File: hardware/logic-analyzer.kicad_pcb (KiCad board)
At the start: 4 copper layers, 39.6 x 40.4 mm, 93 parts, among them J1 USB_C_Receptacle, J2 Conn_02x20, J3 Conn_02x04, J4 Conn_02x15, SW1 SW_Push, SW2 SW_Push, U1 CH32H417MxUx, U16 TPD4EUSB30, U2 Opamp_Dual, U22 TPD4EUSB30, U23 TPD4EUSB30, U3 CH9441P, U4 XC6206PxxxMR, Y1 25MHz 20pF

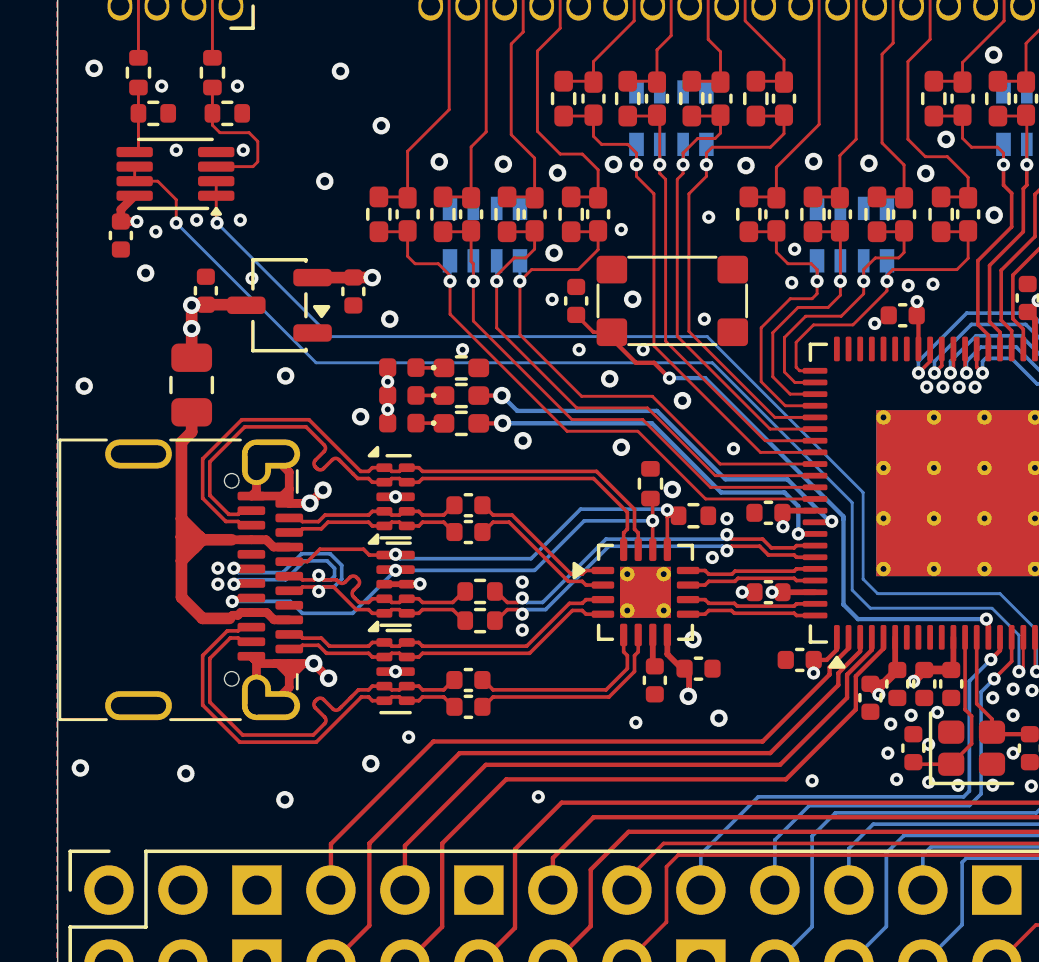
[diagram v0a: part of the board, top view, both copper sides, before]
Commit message: Change CH9441P into something available
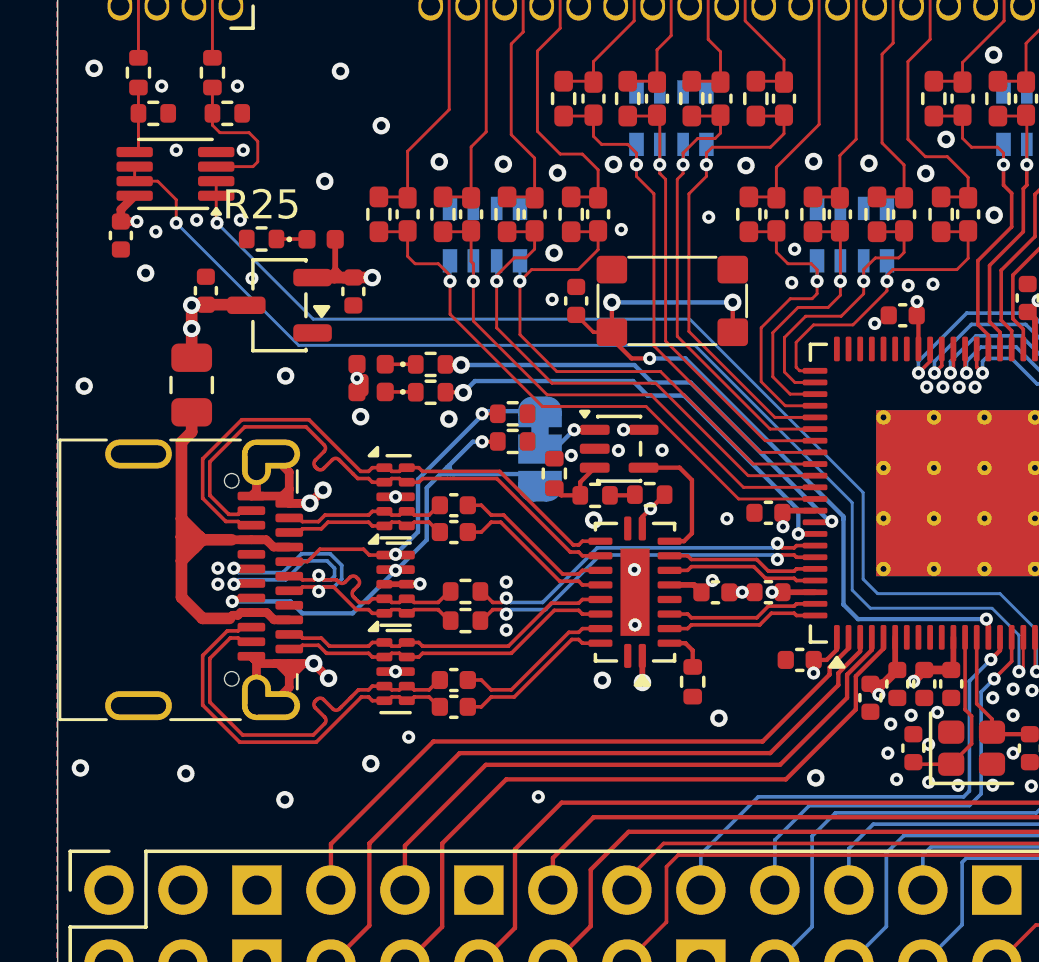
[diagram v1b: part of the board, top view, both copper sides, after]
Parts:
- removed C3: 4.7uF, Capacitor_SMD:C_0402_1005Metric
- added JP1: Sel, Jumper:SolderJumper-3_P1.3mm_Bridged12_RoundedPad1.0x1.5mm, B.Cu at (153.4, 79.0)
- added R26: 5.1k, Resistor_SMD:R_0402_1005Metric, F.Cu at (158.6, 87.0)
- added R27: 5.1k, Resistor_SMD:R_0402_1005Metric, F.Cu at (155.2, 80.5)
- added R28: 5.1k, Resistor_SMD:R_0402_1005Metric, F.Cu at (157.1, 80.5)
- added R29: 1k, Resistor_SMD:R_0402_1005Metric, F.Cu at (153.8, 79.8)
- added U5: TMUXHS4212, Package_DFN_QFN:DHVQFN-20-1EP_2.5x4.5mm_P0.5mm_EP1x3mm, F.Cu at (156.6, 83.9)
- R23, R24, R25: footprint Resistor_SMD:R_0402_1005Metric_Pad0.72x0.64mm_HandSolder -> Resistor_SMD:R_0402_1005Metric
- U3: value CH9441P -> LMV321; footprint Package_DFN_QFN:QFN-16-1EP_3x3mm_P0.5mm_EP1.75x1.75mm_ThermalVias -> Package_TO_SOT_SMD:SOT-353_SC-70-5
- moved R25 8.16 mm to (143.8, 71.8), turned to 0 degrees
- moved R21 7.12 mm to (152.4, 77.8)
- moved D1 5.20 mm to (145.8, 71.8), turned to 0 degrees
- moved U3 5.01 mm to (156.1, 79.0)
- moved R22 4.95 mm to (152.4, 78.7), turned to 0 degrees
- moved C4 3.67 mm to (159.4, 83.9), turned to 0 degrees
- moved D2 1.50 mm to (147.6, 76.0)
- moved D3 1.50 mm to (147.6, 77.0)
- moved R23 1.50 mm to (149.6, 77.0)
- moved R24 1.50 mm to (149.6, 76.1)
- moved C358 0.50 mm to (150.4, 80.9)
- moved C359 0.50 mm to (150.4, 81.8)
- moved C360 0.50 mm to (150.4, 86.9)
- moved C361 0.50 mm to (150.4, 87.8)
- moved R97 0.50 mm to (150.8, 84.8)
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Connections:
- C4 pad 1: Net-(U3-VDD) -> +3V3
- U3 pad 1: /USB1.SSTX1+ -> Net-(JP1-C)
- U3 pad 2: /USB1.SSTX1- -> GND
- U3 pad 3: /USB1.SSRX2- -> Net-(U3--)
- U3 pad 4: /USB1.SSRX2+ -> /SEL
- U3 pad 5: /USB1.SSTX2+ -> +3V3
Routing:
- net +3V3: track 18.2 -> 24.7 mm, vias 8 -> 11
- net /~{RST}: track 21.0 -> 27.2 mm, vias 2 -> 4
- net /SEL: track 0.00 -> 4.54 mm
- net /USB1_CC1: track 16.2 -> 12.9 mm
- net +5V: track 7.75 -> 5.32 mm, vias 4 -> 3
- net Net-(JP1-C): track 0.00 -> 2.15 mm, vias 0 -> 1
- net Net-(U3--): track 0.00 -> 2.15 mm
- net /USB1.SSRX1-: track 21.7 -> 19.7 mm
- net /LED2: track 13.7 -> 15.5 mm
- net /USB1.SSRX1+: track 21.7 -> 20.0 mm
- net /LED1: track 14.5 -> 16.1 mm
- net /USB1.SSTX2-: track 7.03 -> 5.56 mm
- net Net-(U5-~{OE}): track 0.00 -> 1.46 mm
- net Net-(U3-VDD): track 1.11 -> 0.00 mm
- net /USB1.SSTX2+: track 6.63 -> 5.56 mm
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
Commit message: Readme
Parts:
- added TP1: TestPoint_Probe, TestPoint:TestPoint_Pad_D1.5mm, B.Cu at (153.2, 83.1)
- added TP2: TestPoint_Probe, TestPoint:TestPoint_Pad_D1.5mm, B.Cu at (153.2, 85.6)
- added TP3: TestPoint_Probe, TestPoint:TestPoint_Pad_D1.5mm, B.Cu at (153.2, 88.1)
- added TP4: TestPoint_Probe, TestPoint:TestPoint_Pad_D1.5mm, B.Cu at (153.2, 90.6)
- moved JP1 0.71 mm to (152.7, 79.0)
- moved R20 0.70 mm to (141.9, 67.5)
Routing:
- net /USB1_CC1: track 12.9 -> 6.14 mm
- net /CH6: track 9.28 -> 12.2 mm
- net /CH2: track 5.33 -> 8.23 mm
- net /CH10: track 5.36 -> 7.69 mm
- net /USB1_CC2: track 19.5 -> 17.2 mm
- net /CH9: track 5.32 -> 7.50 mm
- net /CH5: track 9.53 -> 11.6 mm
- net /CH1: track 5.26 -> 7.12 mm
- net /CH14: track 9.31 -> 10.9 mm
- net /CH13: track 9.57 -> 11.1 mm
- net /USB1.D+: track 12.7 -> 14.1 mm
- net /USB1.D-: track 12.7 -> 14.1 mm
- net Net-(U2A-+): track 5.28 -> 3.96 mm
- net /CH3: track 5.73 -> 7.05 mm
- net +3V3: track 24.7 -> 25.9 mm, vias 11 -> 12
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
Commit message: Update
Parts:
- removed C22: 100nF, Capacitor_SMD:C_0402_1005Metric
- removed R17: 220R, Resistor_SMD:R_0402_1005Metric
- removed U2: Opamp_Dual, Package_SO:VSSOP-8_2.3x2mm_P0.5mm
- added R30: 100R, Resistor_SMD:R_0402_1005Metric, F.Cu at (142.7, 67.5)
- added R31: 100R, Resistor_SMD:R_0402_1005Metric, F.Cu at (144.6, 67.5)
- added R32: 100R, Resistor_SMD:R_0402_1005Metric, F.Cu at (137.6, 68.1)
- J2: footprint Connector_PinSocket_1.27mm:PinSocket_2x20_P1.27mm_Horizontal -> Connector_PinHeader_1.27mm:PinHeader_2x20_P1.27mm_Horizontal
- J3: footprint Connector_PinSocket_1.27mm:PinSocket_2x04_P1.27mm_Horizontal -> Connector_PinHeader_1.27mm:PinHeader_2x04_P1.27mm_Horizontal
- R20: value 220R -> 100R
- moved J2 24.1 mm to (149.6, 63.8), turned to 90 degrees
- moved J3 3.81 mm to (138.9, 63.8), turned to 90 degrees
- moved R20 2.93 mm to (139.0, 67.6), turned to 180 degrees
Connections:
- J2 pad 10: /CH3 -> GND
- J2 pad 12: GND -> /CH11
- J2 pad 13: +1V8 -> GND
- J2 pad 14: /CH4 -> /CH10
- J2 pad 16: /CH5 -> /CH9
- J2 pad 17: GND -> +3V3
- J2 pad 18: /CH6 -> /CH8
- J2 pad 2: GND -> /CH15
- J2 pad 20: /CH7 -> GND
- J2 pad 22: GND -> /CH7
- J2 pad 23: +3V3 -> GND
- J2 pad 24: /CH8 -> /CH6
- J2 pad 26: /CH9 -> /CH5
- J2 pad 27: GND -> +1V8
- J2 pad 28: /CH10 -> /CH4
- J2 pad 3: +1V8 -> GND
- J2 pad 30: /CH11 -> GND
- J2 pad 32: GND -> /CH3
- J2 pad 33: +3V3 -> GND
- J2 pad 34: /CH12 -> /CH2
- J2 pad 36: /CH13 -> /CH1
- J2 pad 37: GND -> +1V8
- J2 pad 38: /CH14 -> /CH0
- J2 pad 4: /CH0 -> /CH14
- J2 pad 40: /CH15 -> GND
- J2 pad 6: /CH1 -> /CH13
- J2 pad 7: GND -> +3V3
- J2 pad 8: /CH2 -> /CH12
- J3 pad 2: GND -> /ACH1
- J3 pad 4: /ACH0 -> GND
- J3 pad 6: GND -> /ACH0
- J3 pad 8: /ACH1 -> GND
- J4 pad 3: +5V -> /USB1.D+
- J4 pad 5: GND -> /USB1.D-
- R18 pad 2: Net-(U2A-+) -> /A0
- R19 pad 2: Net-(U2B-+) -> /A1
- R20 pad 1: Net-(U2A-+) -> /A1
- R20 pad 2: GND -> Net-(R20-Pad2)
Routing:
- net /USB1.D+: track 14.1 -> 32.2 mm
- net /USB1.D-: track 14.1 -> 32.2 mm
- net /USB1_CC1: track 6.14 -> 12.2 mm
- net Net-(U2A-+): track 3.96 -> 0.00 mm
- net /A0: track 39.7 -> 43.0 mm
- net Net-(U2B-+): track 2.27 -> 0.00 mm
- net /A1: track 42.0 -> 44.2 mm
- net +1V2: track 9.80 -> 11.9 mm
- net +5V: track 5.32 -> 3.69 mm, vias 3 -> 2
- net Net-(R20-Pad2): track 0.00 -> 0.89 mm
- net Net-(R30-Pad2): track 0.00 -> 0.88 mm
- net +3V3: track 25.9 -> 25.5 mm, vias 12 -> 13
- net GND: vias 98 -> 97
- net +1V8: vias 3 -> 4

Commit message: Stencil
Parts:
- added H1: MountingHole, logic-analyzer:Icy Electronics Logo, F.Cu at (146.2, 66.6)
- added H2: MountingHole, logic-analyzer:Icy Electronics Logo, B.Cu at (146.2, 66.6)
- moved R31 3.69 mm to (141.2, 68.9), turned to -90 degrees
- moved R30 1.02 mm to (141.7, 67.5), turned to 180 degrees

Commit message: General improvements
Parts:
- removed R31, R32: 100R, Resistor_SMD:R_0402_1005Metric
- removed TP1, TP2, TP3, TP4: TestPoint_Probe, TestPoint:TestPoint_Pad_D1.5mm
- removed U4: XC6206PxxxMR, Package_TO_SOT_SMD:SOT-23-3
- added C41: 4.7uF, Capacitor_SMD:C_0402_1005Metric, F.Cu at (144.1, 108.9)
- added J5: Conn_02x15, Connector_PinHeader_2.54mm:PinHeader_2x15_P2.54mm_Vertical, F.Cu at (177.8, 94.5)
- added U2: AMS1117-3.3, Package_TO_SOT_SMD:SOT-89-3, F.Cu at (140.5, 107.3)
- J4: footprint Connector_PinSocket_2.54mm:PinSocket_2x15_P2.54mm_Vertical -> Connector_PinHeader_2.54mm:PinHeader_2x15_P2.54mm_Vertical
- moved C40 37.4 mm to (138.3, 110.8), turned to -90 degrees
- moved J4 35.9 mm to (138.7, 130.0)
- moved C39 35.6 mm to (143.2, 108.9)
- moved F2 34.0 mm to (140.5, 110.8), turned to 180 degrees
- moved C33 33.9 mm to (175.6, 115.3), turned to -90 degrees
- moved C27 33.4 mm to (174.9, 113.0)
- moved J2 33.4 mm to (149.7, 97.2)
- moved J3 33.4 mm to (139.1, 97.2)
- moved C1 33.4 mm to (170.3, 122.6)
- moved C10 33.4 mm to (166.0, 104.3)
- moved C11 33.4 mm to (163.8, 104.3)
- moved C12 33.4 mm to (161.6, 104.3)
- moved C13 33.4 mm to (161.9, 100.3)
- moved C14 33.4 mm to (159.7, 100.3)
- moved C15 33.4 mm to (157.5, 100.3)
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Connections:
- J4 pad 1: +5V -> +3V3
- J4 pad 10: /J4 -> /J3
- J4 pad 11: GND -> /J5
- J4 pad 12: /J5 -> GND
- J4 pad 13: /J6 -> /J7
- J4 pad 14: /J7 -> /J6
- J4 pad 15: /J8 -> /J9
- J4 pad 16: /J9 -> /J8
- J4 pad 17: /J10 -> GND
- J4 pad 18: GND -> /J10
- J4 pad 19: /J11 -> /J12
- J4 pad 2: +3V3 -> +5V
- J4 pad 20: /J12 -> /J11
- J4 pad 21: /J13 -> /J14
- J4 pad 22: /J14 -> /J13
- J4 pad 23: /J15 -> /J16
- J4 pad 24: /J16 -> /J15
- J4 pad 25: GND -> /J17
- J4 pad 26: /J17 -> GND
- J4 pad 27: /J18 -> /J19
- J4 pad 28: /J19 -> /J18
- J4 pad 29: /J20 -> GND
- J4 pad 3: /USB1.D+ -> +3V3
- J4 pad 30: GND -> /J20
- J4 pad 4: +3V3 -> /USB1.D+
- J4 pad 5: /USB1.D- -> GND
- J4 pad 6: GND -> /USB1.D-
- J4 pad 7: /J1 -> /J2
- J4 pad 8: /J2 -> /J1
- J4 pad 9: /J3 -> /J4
- R20 pad 2: Net-(R20-Pad2) -> GND
- R30 pad 2: Net-(R30-Pad2) -> GND
- SW2 pad 2: /SW -> /J21
- U1 pad 30: unconnected-(U1-PE14-Pad30) -> /J36
- U1 pad 31: unconnected-(U1-PE15-Pad31) -> /J35
- U1 pad 32: unconnected-(U1-PB10-Pad32) -> /J34
- U1 pad 33: unconnected-(U1-PB11-Pad33) -> /J33
- U1 pad 36: unconnected-(U1-PB12-Pad36) -> /J32
- U1 pad 37: unconnected-(U1-PB13-Pad37) -> /J31
- U1 pad 38: unconnected-(U1-PB14-Pad38) -> /J30
- U1 pad 39: unconnected-(U1-PD10-Pad39) -> /J29
- U1 pad 40: unconnected-(U1-PD11-Pad40) -> /J28
- U1 pad 41: unconnected-(U1-PD12-Pad41) -> /J27
- U1 pad 42: unconnected-(U1-PD13-Pad42) -> /J26
- U1 pad 43: unconnected-(U1-PD14-Pad43) -> /J25
- U1 pad 44: unconnected-(U1-PD15-Pad44) -> /J24
- U1 pad 45: /SW -> /J23
- U1 pad 46: unconnected-(U1-PF1-Pad46) -> /J22
- U1 pad 47: unconnected-(U1-PF2-Pad47) -> /J21
- U1 pad 60: unconnected-(U1-PA14-Pad60) -> /J42
- U1 pad 61: unconnected-(U1-PA15-Pad61) -> /J43
- U1 pad 62: unconnected-(U1-PC10-Pad62) -> /J41
- U1 pad 63: unconnected-(U1-PC11-Pad63) -> /J40
- U1 pad 64: unconnected-(U1-PC12-Pad64) -> /J39
- U1 pad 65: unconnected-(U1-PD0-Pad65) -> /J37
- U1 pad 66: unconnected-(U1-PD1-Pad66) -> /J38
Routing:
- net /J43: track 0.00 -> 30.9 mm, vias 0 -> 1
- net /J40: track 0.00 -> 29.7 mm, vias 0 -> 1
- net /J42: track 0.00 -> 29.4 mm, vias 0 -> 1
- net /J38: track 0.00 -> 29.2 mm, vias 0 -> 1
- net /J41: track 0.00 -> 28.3 mm, vias 0 -> 1
- net /J39: track 0.00 -> 27.0 mm, vias 0 -> 1
- net /J37: track 0.00 -> 26.6 mm, vias 0 -> 1
- net /J21: track 0.00 -> 20.4 mm
- net /J22: track 0.00 -> 18.2 mm
- net /J23: track 0.00 -> 17.6 mm
- net /J24: track 0.00 -> 14.7 mm
- net /J26: track 0.00 -> 12.9 mm
- net /J28: track 0.00 -> 11.5 mm
- net /J33: track 0.00 -> 10.9 mm
- net /J25: track 0.00 -> 10.5 mm
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- added copper zone on F.Cu, net +3V3
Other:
- board size 39.6 x 40.4 mm -> 45.2 x 40.4 mm
- board text added: "3V3 5V 3V3 PB8 GND PB9 PE4 PE3 PE6 PE5 PA0 GND PA5 PA4 PB1 PB2 GND PC0 PA9 PC1 PA11 PA10 PA13 PA12 PE12 GND PE13 PE10 GND PE11"
- board text added: "GND PF2 PF0 PF1 GND PD15 PD14 PD13 PD12 PD11 PD10 GND PB14 PB13 PB12 PB11 GND PB10 PE15 PE14 PD0 PD1 PC12 PC11 PC10 GND PA14 PA15 GND 3V3"
